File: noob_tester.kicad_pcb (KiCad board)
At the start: 2 copper layers, 59.7 x 67.3 mm, 33 parts, among them J1 Conn_01x10_Male, J2 Conn_01x10_Male, J3 Conn_01x10_Male, J4 Conn_01x10_Male, J5 Conn_01x10_Male, J6 Conn_01x10_Male, Q1 Q_NJFET_DGS, Q2 Q_NJFET_DGS, Q3 Q_NJFET_DGS, Q4 Q_NJFET_DGS, U1a LQFP-32_7x7mm_P0.8mm, U1b LQFP-32_7x7mm_P0.8mm

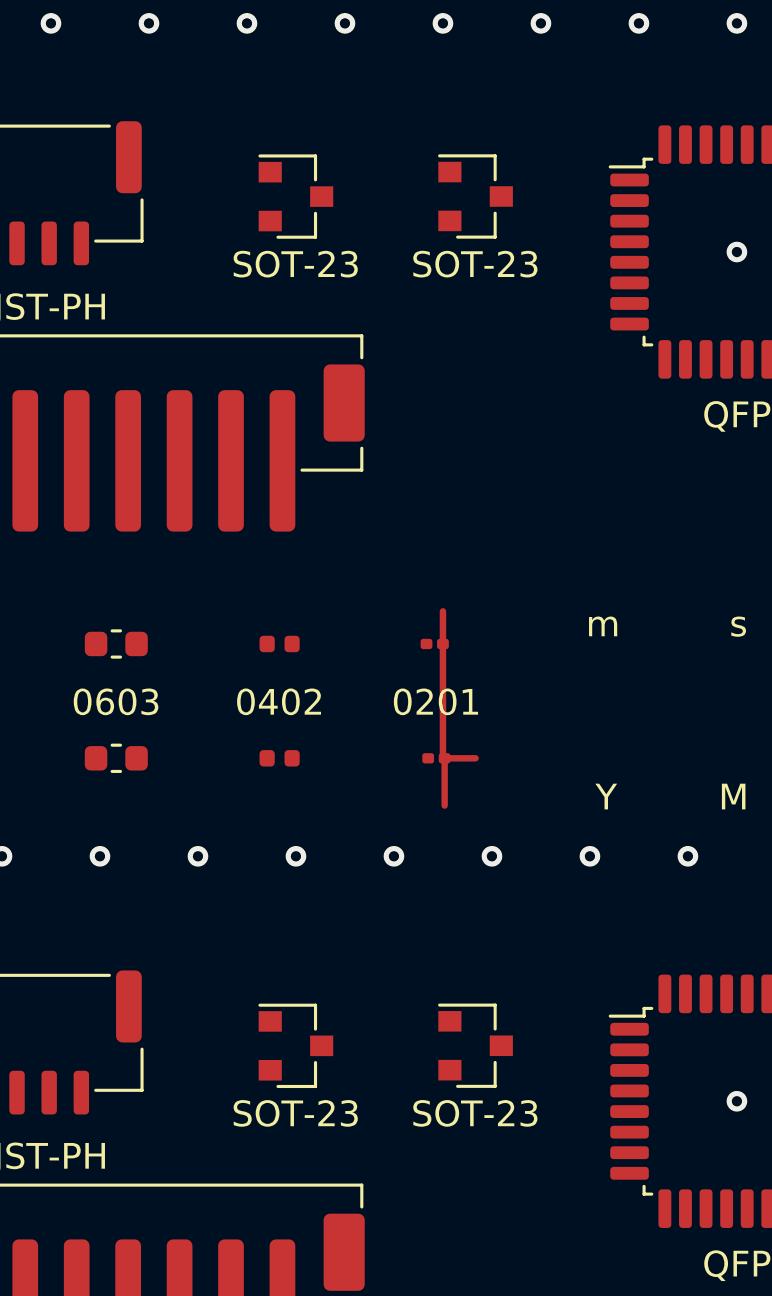
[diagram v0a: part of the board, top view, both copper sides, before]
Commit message: swapped SOT-23 with SOT-723, generated gerber files
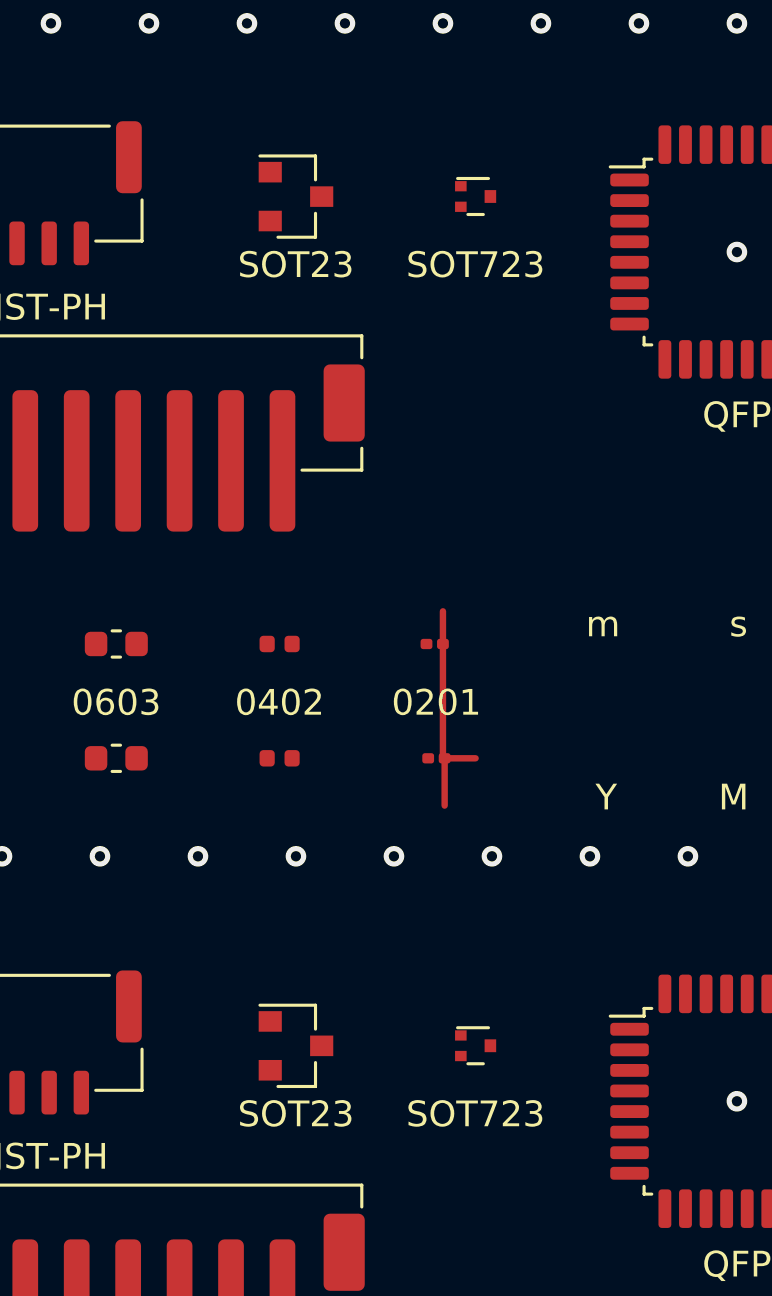
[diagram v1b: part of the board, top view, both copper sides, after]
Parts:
- Q2, Q4: footprint Package_TO_SOT_SMD:SOT-23 -> Package_TO_SOT_SMD:SOT-723
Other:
- board text added: "SOT23"
- board text added: "SOT723"
- board text removed: "SOT-23"
